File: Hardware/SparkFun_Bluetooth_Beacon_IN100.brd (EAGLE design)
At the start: 25.4 x 25.4 mm, 46 parts, among them J3 Vertical Qwiic Connector, U1 IN100, Y1 CRYSTAL-26MHZSMD-3.2X2.5

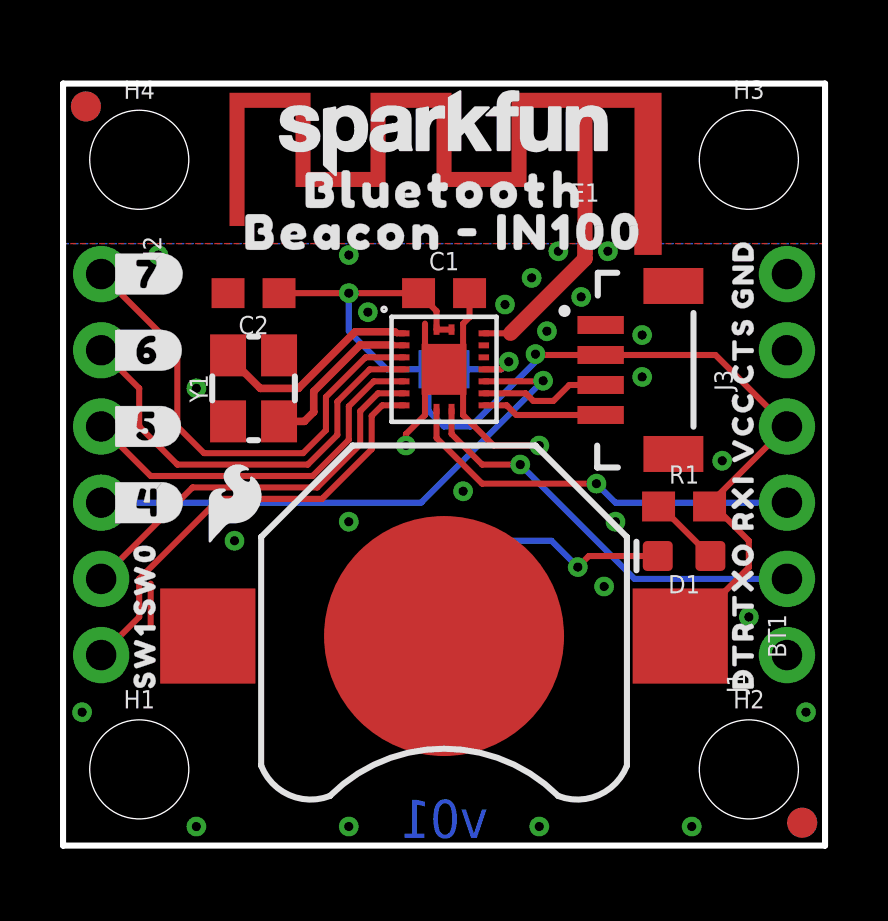
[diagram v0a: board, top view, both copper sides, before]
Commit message: Add suggestions from InPlay
Add diodes to isolate VIN from V_BATT
Add RC filter to EN
Add jumper for I2C power selection
Add bulk capacitor to SW0 output
Reroute entire board to accommodate changes
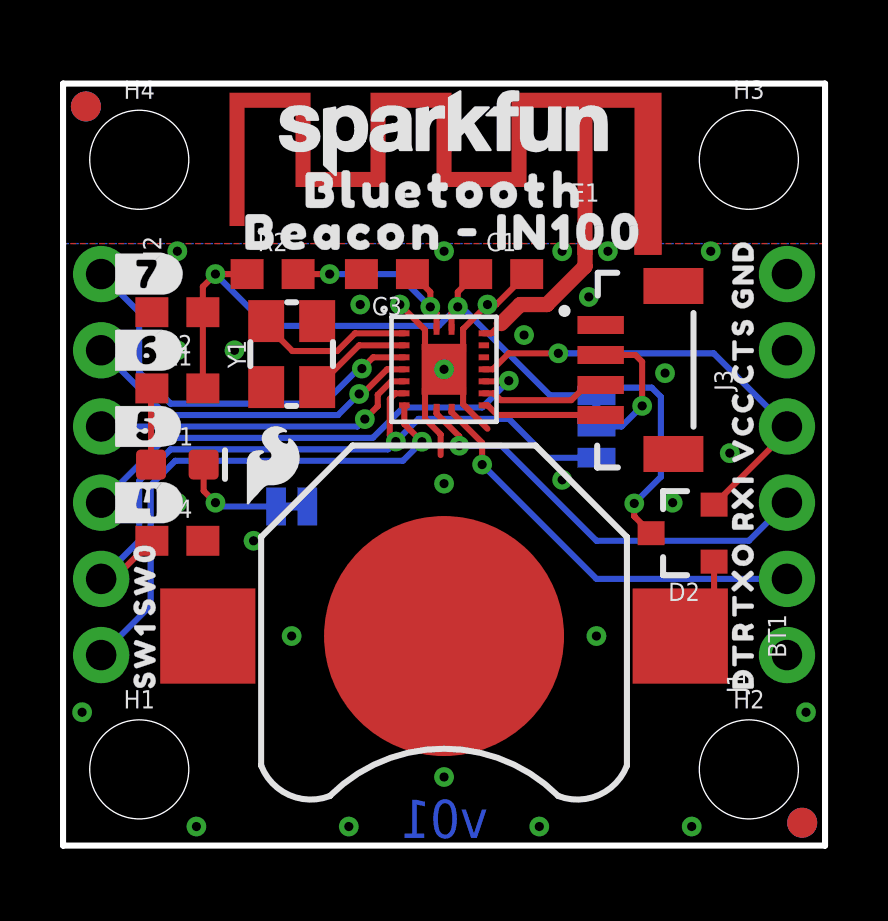
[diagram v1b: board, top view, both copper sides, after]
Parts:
- removed U$11: (no value), output:#VDDQ#0
- removed VDDQ: JUMPER-SMT_2_NC_TRACE_SILK, SparkFun-Jumpers:SMT-JUMPER_2_NC_TRACE_SILK
- added C3: 0.1uF, SparkFun-Capacitors:0603
- added C4: 10uF, SparkFun-Capacitors:0603
- added D2: BAS70-05, SparkFun-DiscreteSemi:SOT23-3
- added JP1: JUMPER-SMT_3_1-NC_TRACE_SILK, SparkFun-Jumpers:SMT-JUMPER_3_1-NC_TRACE_SILK
- added R2: 1k, SparkFun-Resistors:0603
- moved R1 17.3 mm to (3.81, 15.2)
- moved D1 17.2 mm to (3.81, 12.7), turned to 0 degrees
- moved U$19 5.24 mm to (7.62, 13.1)
- moved PWR 5.21 mm to (7.62, 11.3), turned to 0 degrees
- moved LOGO1 5.12 mm to (12.7, 12.1)
- moved C2 2.62 mm to (3.81, 17.8)
- moved C1 2.01 mm to (14.6, 19.1)
- moved U$8 1.80 mm to (6.99, 12.7)
- moved Y1 1.71 mm to (7.62, 16.4)
- moved U$23 1.27 mm to (12.7, 8.89)
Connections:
- new net N$7: J3.2, JP1.2
- new net VIN: D2.2, J1.4, U1.13
- new net V_BATT: BT1.PWR@1, D2.1
- net GND: now also C3.2, C4.2
- net N$3: now also C3.1, R2.2, U1.18; no longer U1.13, VDDQ.1
- net SW0: now also C4.1, JP1.1
- net VCC: now also D2.3, JP1.3, R2.1; no longer BT1.PWR@1, J1.4, J3.2, U1.18, VDDQ.2
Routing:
- net VIN: track 0.00 -> 14.9 mm, vias 0 -> 1
- net SW0: track 13.3 -> 24.7 mm, vias 0 -> 1
- net VCC: track 36.4 -> 29.6 mm, vias 2 -> 3
- net N$7: track 0.00 -> 4.76 mm, vias 0 -> 1
- net N$3: track 2.68 -> 7.04 mm, vias 1 -> 2
- net N$5: track 7.12 -> 3.50 mm
- net V_BATT: track 0.00 -> 2.95 mm
- net IO6: track 14.4 -> 11.6 mm, vias 0 -> 1
- net SW1: track 14.9 -> 17.4 mm, vias 0 -> 1
- net IO7: track 16.0 -> 13.7 mm, vias 0 -> 1
- net IO4: track 18.4 -> 16.1 mm
- net N$2: track 5.64 -> 3.48 mm
- net N$1: track 7.15 -> 5.34 mm
- net IO5: track 12.7 -> 11.0 mm, vias 0 -> 1
- net RX/IO0: track 13.5 -> 14.3 mm
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
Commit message: V10 updates
Bump version number to v10
Extend pads of IN100 to get better fillet outside of chip
Change all 0603 components to 0402
Add I2C pullups
Swap jumper for I2C bus power to make SW0 default
Add I2C test points
Reposition and reroute for above changes
Add silk label to power LED
Remove "Serial" silk from bottom
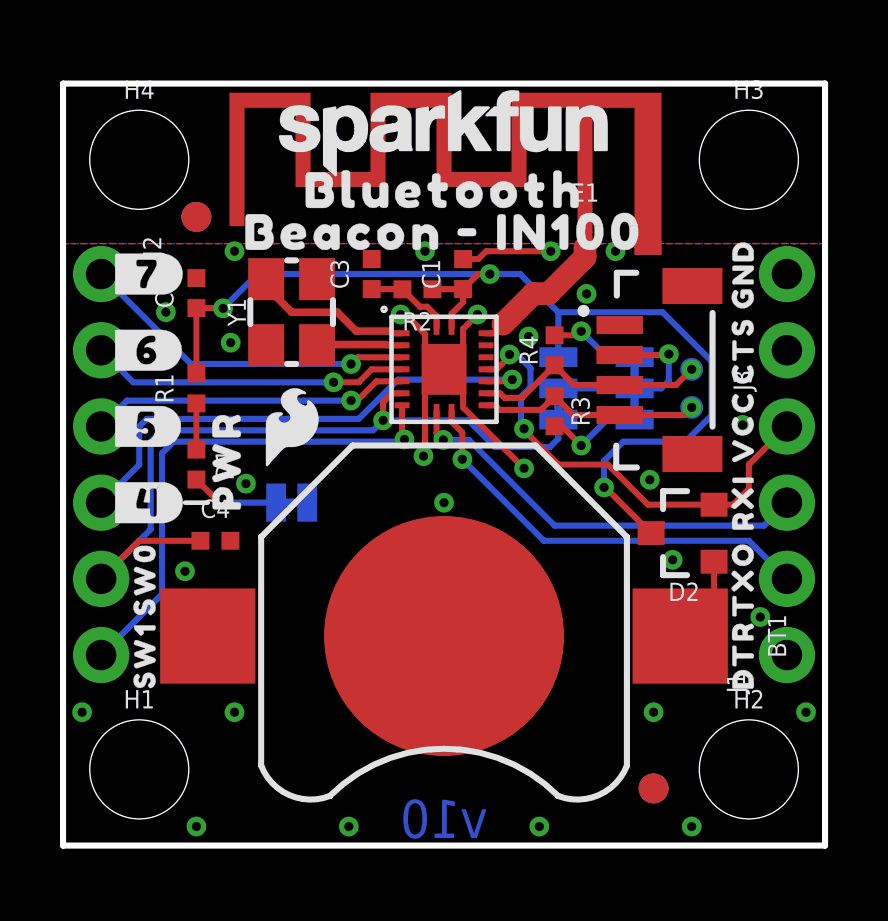
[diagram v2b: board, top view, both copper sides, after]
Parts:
- removed JP1: JUMPER-SMT_3_1-NC_TRACE_SILK, SparkFun-Jumpers:SMT-JUMPER_3_1-NC_TRACE_SILK
- removed U$12: (no value), output:SERIAL0
- added BUS: JUMPER-SMT_3_1-NC_TRACE_SILK, SparkFun-Jumpers:SMT-JUMPER_3_1-NC_TRACE_SILK
- added I2C: JUMPER-SMT_3_2-NC_TRACE_SILK, SparkFun-Jumpers:SMT-JUMPER_3_2-NC_TRACE_SILK
- added R3, R4: 2.2k, SparkFun-Resistors:0402-TIGHT
- added TP1, TP2: TEST-POINT3, SparkFun-Connectors:PAD.03X.03
- added U$11: (no value), output:#I2C#0
- added U$20: (no value), output:#SW0#3
- added U$24: (no value), output:#VCC#0
- added U$25: (no value), output:#BUS#0
- added U$26: (no value), output:PWR0
- C1, C2, C3, C4: device SparkFun-Capacitors:0603 -> SparkFun-Capacitors:0402-TIGHT
- D1: device SparkFun-LED:LED-0603 -> SparkFun-LED:LED-0402
- R1: value 1k -> 2.2k; device SparkFun-Resistors:0603 -> SparkFun-Resistors:0402-TIGHT
- R2: device SparkFun-Resistors:0603 -> SparkFun-Resistors:0402-TIGHT
- moved FD1 5.21 mm to (4.45, 21.0)
- moved FD2 5.21 mm to (4.45, 21.0)
- moved FD3 5.08 mm to (19.7, 1.91)
- moved FD4 5.08 mm to (19.7, 1.91)
- moved R2 4.85 mm to (11.8, 18.5), turned to 180 degrees
- moved U$8 1.42 mm to (7.62, 14.0)
- moved Y1 1.40 mm to (7.62, 17.8)
- moved C4 1.27 mm to (5.08, 10.2)
- moved C1 1.27 mm to (13.3, 19.1), turned to 90 degrees
- moved C2 0.90 mm to (4.45, 18.4), turned to 90 degrees
- moved J3 0.64 mm to (17.8, 15.9)
- moved D1 0.64 mm to (4.45, 12.7), turned to 270 degrees
- moved R1 0.64 mm to (4.45, 15.2), turned to 90 degrees
- moved LOGO1 0.63 mm to (12.7, 11.4)
- moved C3 0.51 mm to (10.3, 19.1), turned to 90 degrees
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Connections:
- new net N$8: BUS.2, I2C.2, J3.2
- new net N$9: I2C.3, R3.2
- net N$7: now also I2C.1, R4.2; no longer J3.2, JP1.2
- net SCL/IO2: now also R3.1, TP2.1
- net SDA/IO3: now also R4.1, TP1.1
- net SW0: now also BUS.3; no longer JP1.1
- net VCC: now also BUS.1; no longer JP1.3
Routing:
- net N$8: track 0.00 -> 6.33 mm, vias 0 -> 1
- net VCC: track 29.6 -> 35.2 mm
- net N$3: track 7.04 -> 2.91 mm, vias 2 -> 0
- net SDA/IO3: track 4.20 -> 7.86 mm, vias 0 -> 1
- net SCL/IO2: track 4.03 -> 7.47 mm, vias 0 -> 1
- net N$9: track 0.00 -> 3.29 mm, vias 0 -> 1
- net IO7: track 13.7 -> 11.4 mm
- net GND: track 13.2 -> 15.4 mm, vias 29 -> 27
- net N$7: track 4.76 -> 3.08 mm
- net N$6: track 2.55 -> 1.54 mm
- net IO6: track 11.6 -> 10.7 mm
- net IO4: track 16.1 -> 17.0 mm
- net SW0: track 24.7 -> 25.4 mm
- net N$2: track 3.48 -> 2.85 mm
- net VIN: track 14.9 -> 15.5 mm, vias 1 -> 2
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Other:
- board text added: "v10"
- board text removed: "v01"

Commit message: Design review updates
Remove power management diodes
Space out I2C test points
Increase VCC and SW0 net widths to 16 mil
Move crystal to avoid interference from VCC trace underneath
Change "Board info" silk to "Notes"
Add measures for coin cell
Add note in schematic to use CR1225 battery
Add warning in schematic and silk to remove battery when powering with VCC
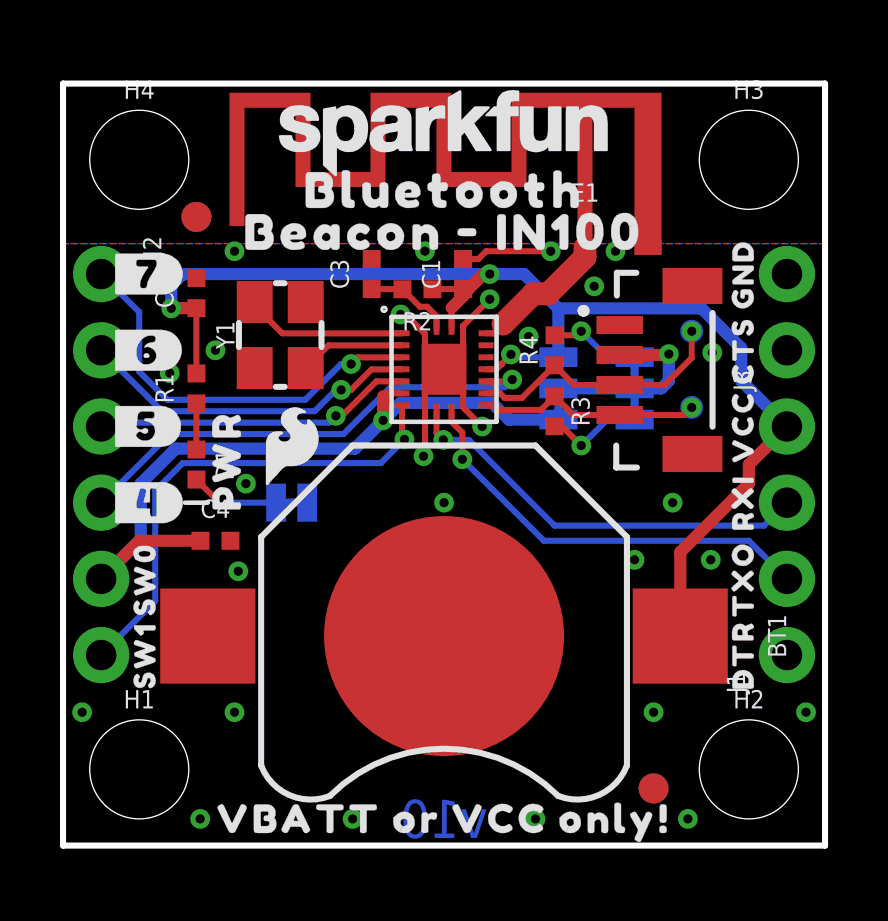
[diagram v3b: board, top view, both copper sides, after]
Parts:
- removed D2: BAS70-05, SparkFun-DiscreteSemi:SOT23-3
- removed U$23: (no value), output:#BOARD_INFO#0
- added U$12: (no value), output:#NOTES#0
- added U$27: (no value), output:VBATT_OR_VCC_ONLY##0
- moved FRAME1 3.81 mm to (-10.2, -25.4)
- moved TP1 1.27 mm to (21.0, 17.1)
- moved Y1 0.85 mm to (7.24, 17.0)
- moved U$8 0.63 mm to (7.62, 13.3)
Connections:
- removed net VIN: D2.2, J1.4, U1.13
- removed net V_BATT: BT1.PWR@1, D2.1
- net VCC: now also BT1.PWR@1, J1.4, U1.13; no longer D2.3
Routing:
- net VIN: track 15.5 -> 0.00 mm, vias 2 -> 0
- net VCC: track 35.2 -> 43.5 mm
- net V_BATT: track 2.95 -> 0.00 mm
- net IO7: track 11.4 -> 13.5 mm
- net GND: track 15.4 -> 14.1 mm
- net SW0: track 25.4 -> 24.3 mm
- net SDA/IO3: track 7.86 -> 8.90 mm
- net IO6: track 10.7 -> 11.5 mm
- net IO4: track 17.0 -> 16.3 mm
- net N$2: track 2.85 -> 3.52 mm
- net SW1: track 17.0 -> 16.4 mm

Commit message: v10 updates
Add reset button
Remove SW0 capacitor
Remove top mounting holes
Add solder pads to identify development / production SKUs
Add Qwiic logo
Increase SFE flame silk logo
Nudge Qwiic connector and test points down 25 mils
Move power LED and EN resistor to left side of battery holder
Move VCC trace away from under RF trace
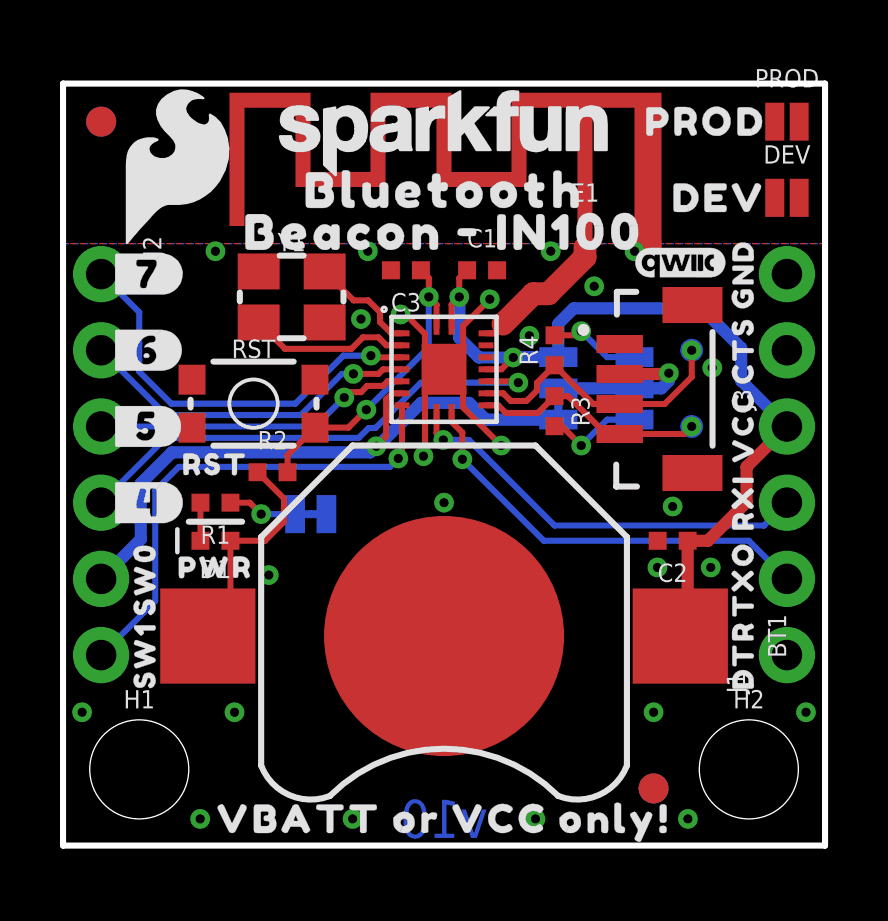
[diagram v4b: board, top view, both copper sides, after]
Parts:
- removed C4: 10uF, SparkFun-Capacitors:0402-TIGHT
- removed H3, H4: STAND-OFF, SparkFun-Hardware:STAND-OFF
- added DEV, PROD: JUMPER-SMT_2_NC_PASTE_NO-SILK, SparkFun-Jumpers:SMT-JUMPER_2_NC_PASTE_NO-SILK
- added LOGO3: QWIIC_LOGO_3MM, SparkFun-Aesthetics:QWIIC_3MM
- added RST: MOMENTARY-SWITCH-SPST-SMD-4.6X2.8MM, SparkFun-Switches:TACTILE_SWITCH_SMD_4.6X2.8MM
- added U$23: (no value), output:RST0
- added U$28: (no value), output:DEV0
- added U$29: (no value), output:PROD0
- U$8: device SparkFun-Aesthetics:SFE_LOGO_FLAME_.1 -> SparkFun-Aesthetics:SFE_LOGO_FLAME_.2
- moved C2 17.9 mm to (20.3, 10.2), turned to 180 degrees
- moved U$8 10.0 mm to (3.81, 22.6)
- moved R2 7.78 mm to (6.99, 12.4), turned to 0 degrees
- moved FD1 4.49 mm to (1.27, 24.1)
- moved FD2 4.49 mm to (1.27, 24.1)
- moved R1 3.86 mm to (5.08, 11.4), turned to 180 degrees
- moved U$26 3.58 mm to (5.08, 9.27), turned to 0 degrees
- moved D1 2.62 mm to (5.08, 10.2), turned to 180 degrees
- moved Y1 1.33 mm to (7.62, 18.3), turned to 0 degrees
- moved C3 1.15 mm to (11.4, 19.2), turned to 180 degrees
- moved PWR 0.74 mm to (8.26, 11.0)
- moved U$19 0.74 mm to (8.26, 12.7)
- moved C1 0.65 mm to (14.0, 19.2), turned to 0 degrees
- moved J3 0.63 mm to (17.8, 15.2)
- moved TP2 0.63 mm to (21.0, 14.0)
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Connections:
- removed net N$6: D1.A, R1.1
- new net EN: C3.1, R2.2, RST.1, RST.2, U1.18
- net GND: now also RST.3, RST.4; no longer C4.2
- net N$3: now also PWR.2, R1.1; no longer C3.1, R2.2, U1.18
- net N$5: now also R1.2; no longer PWR.2
- net SW0: no longer C4.1
- net VCC: now also BT1.PWR@2, D1.A; no longer R1.2
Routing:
- net EN: track 0.00 -> 10.6 mm, vias 0 -> 2
- net VCC: track 43.5 -> 35.8 mm, vias 3 -> 2
- net SW0: track 24.3 -> 21.3 mm
- net GND: track 14.1 -> 12.0 mm, vias 27 -> 25
- net N$2: track 3.52 -> 5.41 mm
- net N$1: track 5.42 -> 3.63 mm
- net N$5: track 2.97 -> 1.27 mm, vias 1 -> 0
- net N$6: track 1.54 -> 0.00 mm
- net N$8: track 6.33 -> 5.69 mm
- net N$3: track 2.91 -> 2.31 mm, vias 0 -> 1
